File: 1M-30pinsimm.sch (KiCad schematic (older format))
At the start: 9 parts, among them U1 JEDEC-FPDRAM, U2 JEDEC-FPDRAM, U3 JEDEC-FPDRAM_Parity

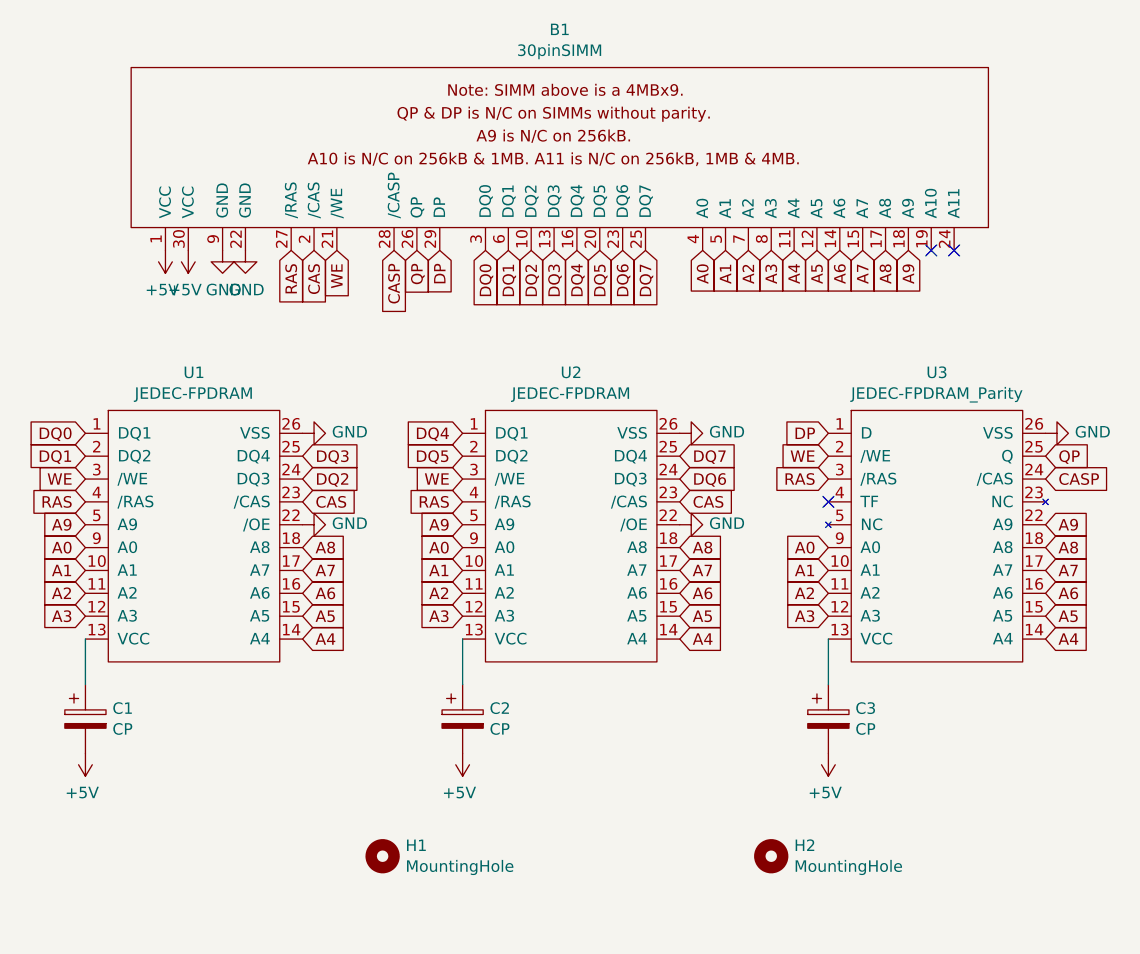
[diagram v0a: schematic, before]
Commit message: change caps
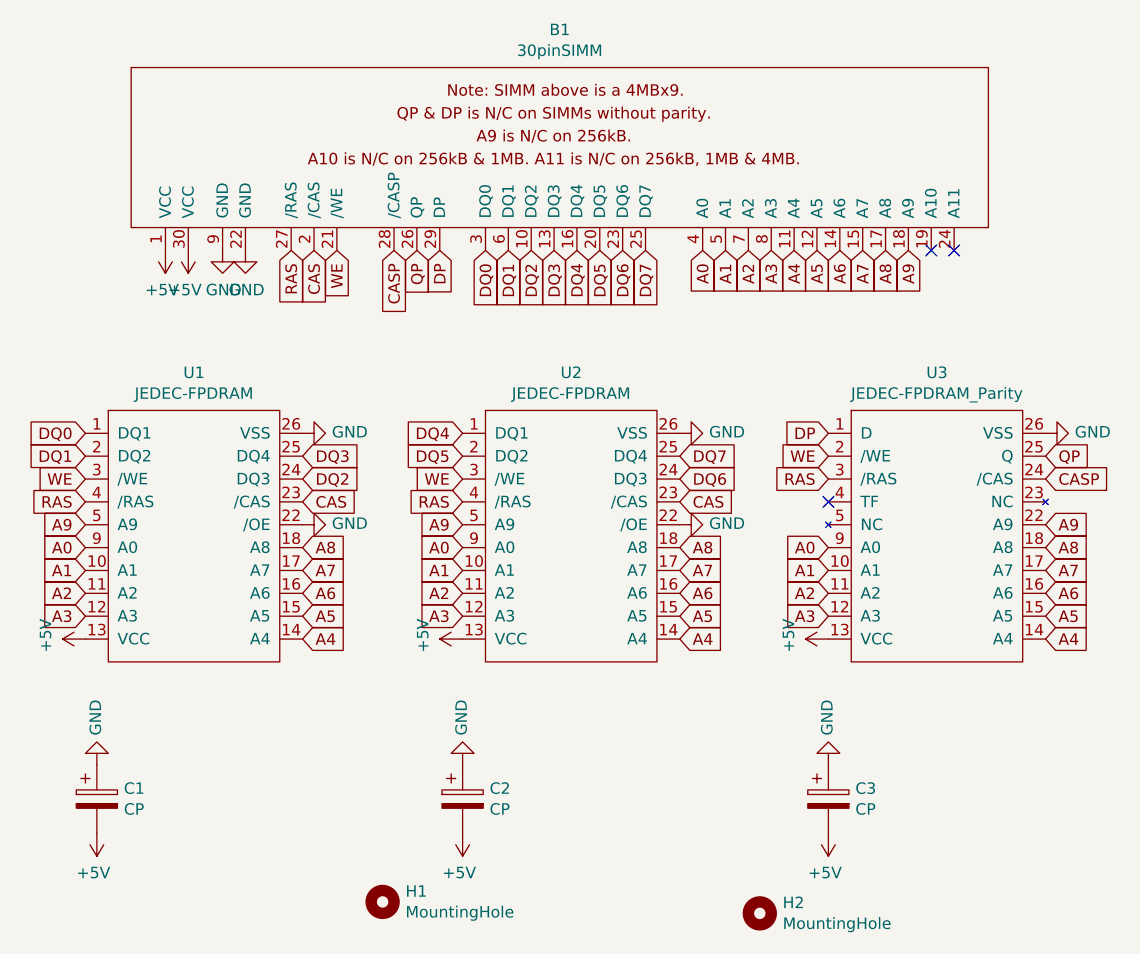
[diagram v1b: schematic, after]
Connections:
- net +5V: now also U1.13 (VCC), U2.13 (VCC), U3.13 (VCC)
- net GND: now also C1.1, C2.1, C3.1
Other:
- moved on the sheet: C1, C2, C3, H1, H2
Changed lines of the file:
@@
 L Mechanical:MountingHole H1
 U 1 1 5FFE89F8
-P 4900 4900
-F 0 "H1" H 5000 4946 50  0000 L CNN
-F 1 "MountingHole" H 5000 4855 50  0000 L CNN
-F 2 "Mounting_Holes:MountingHole_3.2mm_M3" H 4900 4900 50  0001 C CNN
-F 3 "~" H 4900 4900 50  0001 C CNN
-	1    4900 4900
+P 4900 5100
+F 0 "H1" H 5000 5146 50  0000 L CNN
+F 1 "MountingHole" H 5000 5055 50  0000 L CNN
+F 2 "Mounting_Holes:MountingHole_3.2mm_M3" H 4900 5100 50  0001 C CNN
+F 3 "~" H 4900 5100 50  0001 C CNN
+	1    4900 5100
 	1    0    0    -1
 $EndComp
@@
 L Mechanical:MountingHole H2
 U 1 1 5FFE8F8D
-P 6600 4900
-F 0 "H2" H 6700 4946 50  0000 L CNN
-F 1 "MountingHole" H 6700 4855 50  0000 L CNN
-F 2 "Mounting_Holes:MountingHole_3.2mm_M3" H 6600 4900 50  0001 C CNN
-F 3 "~" H 6600 4900 50  0001 C CNN
-	1    6600 4900
+P 6550 5150
+F 0 "H2" H 6650 5196 50  0000 L CNN
+F 1 "MountingHole" H 6650 5105 50  0000 L CNN
+F 2 "Mounting_Holes:MountingHole_3.2mm_M3" H 6550 5150 50  0001 C CNN
+F 3 "~" H 6550 5150 50  0001 C CNN
+	1    6550 5150
 	1    0    0    -1
 $EndComp
@@
 L Device:CP C1
 U 1 1 5FFEBDF2
-P 3600 4300
-F 0 "C1" H 3718 4346 50  0000 L CNN
-F 1 "CP" H 3718 4255 50  0000 L CNN
-F 2 "Capacitors_SMD:C_0805_HandSoldering" H 3638 4150 50  0001 C CNN
-F 3 "~" H 3600 4300 50  0001 C CNN
-	1    3600 4300
+P 3650 4650
+F 0 "C1" H 3768 4696 50  0000 L CNN
+F 1 "CP" H 3768 4605 50  0000 L CNN
+F 2 "Capacitors_SMD:C_0805_HandSoldering" H 3688 4500 50  0001 C CNN
+F 3 "~" H 3650 4650 50  0001 C CNN
+	1    3650 4650
 	1    0    0    -1
 $EndComp
@@
 L Device:CP C2
 U 1 1 5FFEC894
-P 5250 4300
-F 0 "C2" H 5368 4346 50  0000 L CNN
-F 1 "CP" H 5368 4255 50  0000 L CNN
-F 2 "Capacitors_SMD:C_0805_HandSoldering" H 5288 4150 50  0001 C CNN
-F 3 "~" H 5250 4300 50  0001 C CNN
-	1    5250 4300
+P 5250 4650
+F 0 "C2" H 5368 4696 50  0000 L CNN
+F 1 "CP" H 5368 4605 50  0000 L CNN
+F 2 "Capacitors_SMD:C_0805_HandSoldering" H 5288 4500 50  0001 C CNN
+F 3 "~" H 5250 4650 50  0001 C CNN
+	1    5250 4650
 	1    0    0    -1
 $EndComp
@@
 L power:+5V #PWR0109
 U 1 1 5FFED258
-P 3600 4450
-F 0 "#PWR0109" H 3600 4300 50  0001 C CNN
-F 1 "+5V" H 3615 4623 50  0000 C CNN
-F 2 "" H 3600 4450 50  0001 C CNN
-F 3 "" H 3600 4450 50  0001 C CNN
-	1    3600 4450
+P 3650 4800
+F 0 "#PWR0109" H 3650 4650 50  0001 C CNN
+F 1 "+5V" H 3665 4973 50  0000 C CNN
+F 2 "" H 3650 4800 50  0001 C CNN
+F 3 "" H 3650 4800 50  0001 C CNN
+	1    3650 4800
 	-1   0    0    1
 $EndComp
@@
 L power:+5V #PWR0110
 U 1 1 5FFED831
-P 5250 4450
-F 0 "#PWR0110" H 5250 4300 50  0001 C CNN
-F 1 "+5V" H 5265 4623 50  0000 C CNN
-F 2 "" H 5250 4450 50  0001 C CNN
-F 3 "" H 5250 4450 50  0001 C CNN
-	1    5250 4450
-	-1   0    0    1
-$EndComp
-Wire Wire Line
-	3600 4150 3600 3950
-Wire Wire Line
-	5250 4150 5250 3950
+P 5250 4800
+F 0 "#PWR0110" H 5250 4650 50  0001 C CNN
+F 1 "+5V" H 5265 4973 50  0000 C CNN
+F 2 "" H 5250 4800 50  0001 C CNN
+F 3 "" H 5250 4800 50  0001 C CNN
+	1    5250 4800
+	-1   0    0    1
+$EndComp
 Text GLabel 6850 3850 0    50   Input ~ 0
 A3
@@
 L Device:CP C3
 U 1 1 5FFFE8F4
-P 6850 4300
-F 0 "C3" H 6968 4346 50  0000 L CNN
-F 1 "CP" H 6968 4255 50  0000 L CNN
-F 2 "Capacitors_SMD:C_0805_HandSoldering" H 6888 4150 50  0001 C CNN
-F 3 "~" H 6850 4300 50  0001 C CNN
-	1    6850 4300
+P 6850 4650
+F 0 "C3" H 6968 4696 50  0000 L CNN
+F 1 "CP" H 6968 4605 50  0000 L CNN
+F 2 "Capacitors_SMD:C_0805_HandSoldering" H 6888 4500 50  0001 C CNN
+F 3 "~" H 6850 4650 50  0001 C CNN
+	1    6850 4650
 	1    0    0    -1
 $EndComp
@@
 L power:+5V #PWR0111
 U 1 1 5FFFF5A4
-P 6850 4450
-F 0 "#PWR0111" H 6850 4300 50  0001 C CNN
-F 1 "+5V" H 6865 4623 50  0000 C CNN
-F 2 "" H 6850 4450 50  0001 C CNN
-F 3 "" H 6850 4450 50  0001 C CNN
-	1    6850 4450
-	-1   0    0    1
-$EndComp
-Wire Wire Line
-	6850 4150 6850 3950
+P 6850 4800
+F 0 "#PWR0111" H 6850 4650 50  0001 C CNN
+F 1 "+5V" H 6865 4973 50  0000 C CNN
+F 2 "" H 6850 4800 50  0001 C CNN
+F 3 "" H 6850 4800 50  0001 C CNN
+	1    6850 4800
+	-1   0    0    1
+$EndComp
 NoConn ~ 6850 3350
 $Comp
@@
 	0    -1   -1   0
 $EndComp
+$Comp
+L power:+5V #PWR?
+U 1 1 60036340
+P 3600 3950
+F 0 "#PWR?" H 3600 3800 50  0001 C CNN
+F 1 "+5V" H 3615 4123 50  0000 C CNN
+F 2 "" H 3600 3950 50  0001 C CNN
+F 3 "" H 3600 3950 50  0001 C CNN
+	1    3600 3950
+	0    -1   -1   0
+$EndComp
+$Comp
+L power:GND #PWR?
+U 1 1 60036C40
+P 3650 4500
+F 0 "#PWR?" H 3650 4250 50  0001 C CNN
+F 1 "GND" V 3655 4372 50  0000 R CNN
+F 2 "" H 3650 4500 50  0001 C CNN
+F 3 "" H 3650 4500 50  0001 C CNN
+	1    3650 4500
+	-1   0    0    1
+$EndComp
+$Comp
+L power:GND #PWR?
+U 1 1 60038BE4
+P 5250 4500
+F 0 "#PWR?" H 5250 4250 50  0001 C CNN
+F 1 "GND" V 5255 4372 50  0000 R CNN
+F 2 "" H 5250 4500 50  0001 C CNN
+F 3 "" H 5250 4500 50  0001 C CNN
+	1    5250 4500
+	-1   0    0    1
+$EndComp
+$Comp
+L power:+5V #PWR?
+U 1 1 600392F7
+P 5250 3950
+F 0 "#PWR?" H 5250 3800 50  0001 C CNN
+F 1 "+5V" H 5265 4123 50  0000 C CNN
+F 2 "" H 5250 3950 50  0001 C CNN
+F 3 "" H 5250 3950 50  0001 C CNN
+	1    5250 3950
+	0    -1   -1   0
+$EndComp
+$Comp
+L power:GND #PWR?
+U 1 1 6003A8D9
+P 6850 4500
+F 0 "#PWR?" H 6850 4250 50  0001 C CNN
+F 1 "GND" V 6855 4372 50  0000 R CNN
+F 2 "" H 6850 4500 50  0001 C CNN
+F 3 "" H 6850 4500 50  0001 C CNN
+	1    6850 4500
+	-1   0    0    1
+$EndComp
+$Comp
+L power:+5V #PWR?
+U 1 1 6003AEEF
+P 6850 3950
+F 0 "#PWR?" H 6850 3800 50  0001 C CNN
+F 1 "+5V" H 6865 4123 50  0000 C CNN
+F 2 "" H 6850 3950 50  0001 C CNN
+F 3 "" H 6850 3950 50  0001 C CNN
+	1    6850 3950
+	0    -1   -1   0
+$EndComp
